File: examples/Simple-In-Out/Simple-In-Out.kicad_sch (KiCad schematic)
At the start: 2 parts, among them J1 IN, J2 OUT

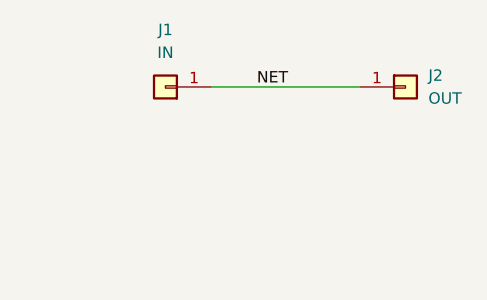
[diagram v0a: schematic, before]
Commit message: Add GND net and vias
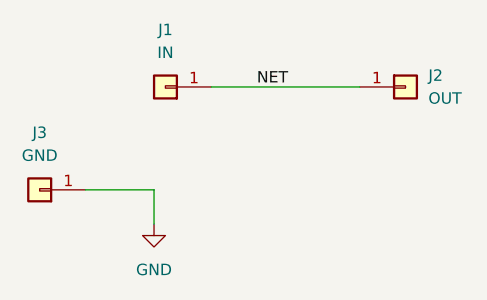
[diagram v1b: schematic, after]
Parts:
- added J3: GND, Connector_PinHeader_2.54mm:PinHeader_1x01_P2.54mm_Vertical, symbol Connector_Generic:Conn_01x01
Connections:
- new net GND: J3.1 (Pin_1)
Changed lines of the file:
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@@
+	(wire
+		(pts
+			(xy 60.96 85.09) (xy 68.58 85.09)
+		)
+		(stroke
+			(width 0)
+			(type default)
+		)
+	)
+	(wire
+		(pts
+			(xy 68.58 85.09) (xy 68.58 88.9)
+		)
+		(stroke
+			(width 0)
+			(type default)
+		)
+	)
 	(wire
 		(pts
@@
 			)
 			(justify left bottom)
+		)
+	)
+	(symbol
+		(lib_id "Connector_Generic:Conn_01x01")
+		(at 55.88 85.09 180)
+		(unit 1)
+		(body_style 1)
+		(exclude_from_sim no)
+		(in_bom yes)
+		(on_board yes)
+		(in_pos_files yes)
+		(dnp no)
+		(fields_autoplaced yes)
+		(property "Reference" "J3"
+			(at 55.88 78.74 0)
+			(show_name no)
+			(do_not_autoplace no)
+			(effects
+				(font
+					(size 1.27 1.27)
+				)
+			)
+		)
+		(property "Value" "GND"
+			(at 55.88 81.28 0)
+			(show_name no)
+			(do_not_autoplace no)
+			(effects
+				(font
+					(size 1.27 1.27)
+				)
+			)
+		)
+		(property "Footprint" "Connector_PinHeader_2.54mm:PinHeader_1x01_P2.54mm_Vertical"
+			(at 55.88 85.09 0)
+			(hide yes)
+			(show_name no)
+			(do_not_autoplace no)
+			(effects
+				(font
+					(size 1.27 1.27)
+				)
+			)
+		)
+		(property "Datasheet" ""
+			(at 55.88 85.09 0)
+			(hide yes)
+			(show_name no)
+			(do_not_autoplace no)
+			(effects
+				(font
+					(size 1.27 1.27)
+				)
+			)
+		)
+		(property "Description" "Generic connector, single row, 01x01, script generated (kicad-library-utils/schlib/autogen/connector/)"
+			(at 55.88 85.09 0)
+			(hide yes)
+			(show_name no)
+			(do_not_autoplace no)
+			(effects
+				(font
+					(size 1.27 1.27)
+				)
+			)
+		)
+		(pin "1"
+		)
+		(instances
+			(project "Simple-In-Out"
+				(path "/b62f0465-5c19-4dba-b4c3-b9525ca01d25"
+					(reference "J3")
+					(unit 1)
+				)
+			)
 		)
 	)
@@
 					(unit 1)
 				)
+			)
+		)
+	)
+	(symbol
+		(lib_id "power:GND")
+		(at 68.58 88.9 0)
+		(unit 1)
+		(body_style 1)
+		(exclude_from_sim no)
+		(in_bom yes)
+		(on_board yes)
+		(in_pos_files yes)
+		(dnp no)
+		(fields_autoplaced yes)
+		(property "Reference" "#PWR01"
+			(at 68.58 95.25 0)
+			(hide yes)
+			(show_name no)
+			(do_not_autoplace no)
+			(effects
+				(font
+					(size 1.27 1.27)
+				)
+			)
+		)
+		(property "Value" "GND"
+			(at 68.58 93.98 0)
+			(show_name no)
+			(do_not_autoplace no)
+			(effects
+				(font
+					(size 1.27 1.27)
+				)
+			)
+		)
+		(property "Footprint" ""
+			(at 68.58 88.9 0)
+			(hide yes)
+			(show_name no)
+			(do_not_autoplace no)
+			(effects
+				(font
+					(size 1.27 1.27)
+				)
+			)
+		)
+		(property "Datasheet" ""
+			(at 68.58 88.9 0)
+			(hide yes)
+			(show_name no)
+			(do_not_autoplace no)
+			(effects
+				(font
+					(size 1.27 1.27)
+				)
+			)
+		)
+		(property "Description" "Power symbol creates a global label with name \"GND\" , ground"
+			(at 68.58 88.9 0)
+			(hide yes)
+			(show_name no)
+			(do_not_autoplace no)
+			(effects
+				(font
+					(size 1.27 1.27)
+				)
+			)
+		)
+		(pin "1"
+		)
+		(instances
+			(project "Simple-In-Out"
+				(path "/b62f0465-5c19-4dba-b4c3-b9525ca01d25"
+					(reference "#PWR01")
+					(unit 1)
+				)
